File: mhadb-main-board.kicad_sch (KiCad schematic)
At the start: 62 parts, among them J1 Conn_01x04_Pin, J2 USB_C_Receptacle_USB2.0_14P, J3 Conn_01x04, J4 Conn_01x04, J5 Conn_01x04, J6 Conn_01x02, SW1 SW_Push, SW2 SW_Push, U1 ESP32-S3FN8, U2 SN65HVD230, U6 TPS5430DDA, U9 LDL212PV33R, Y1 48M

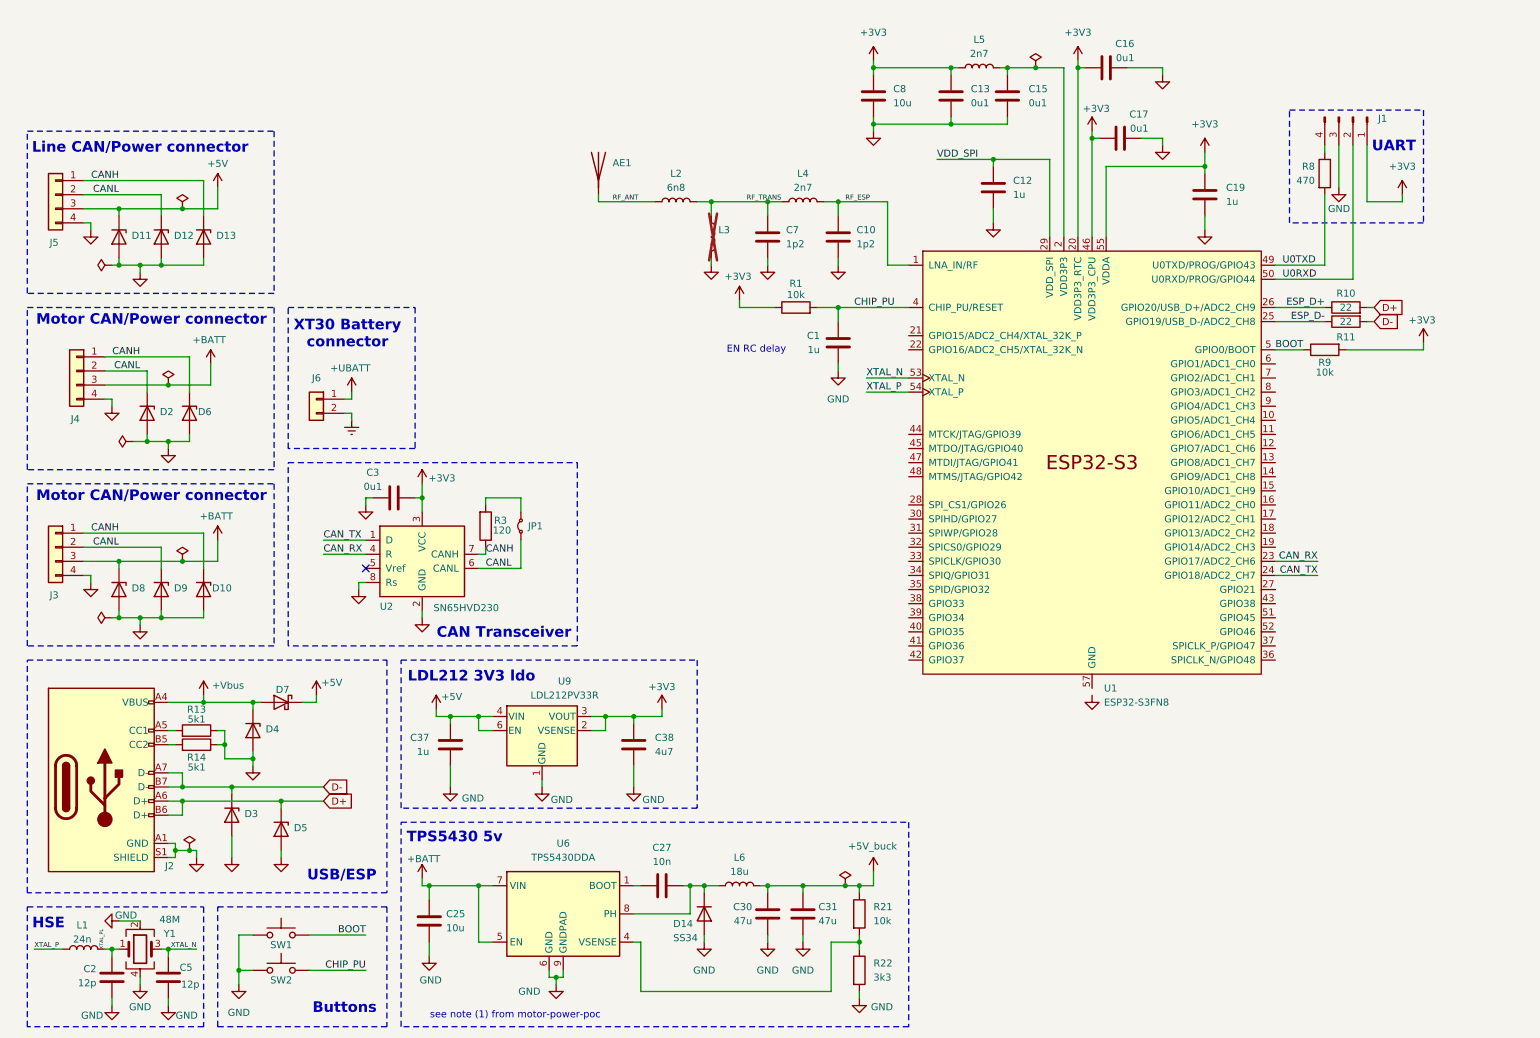
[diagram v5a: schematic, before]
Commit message: schem: import BQ77905 Battery protection
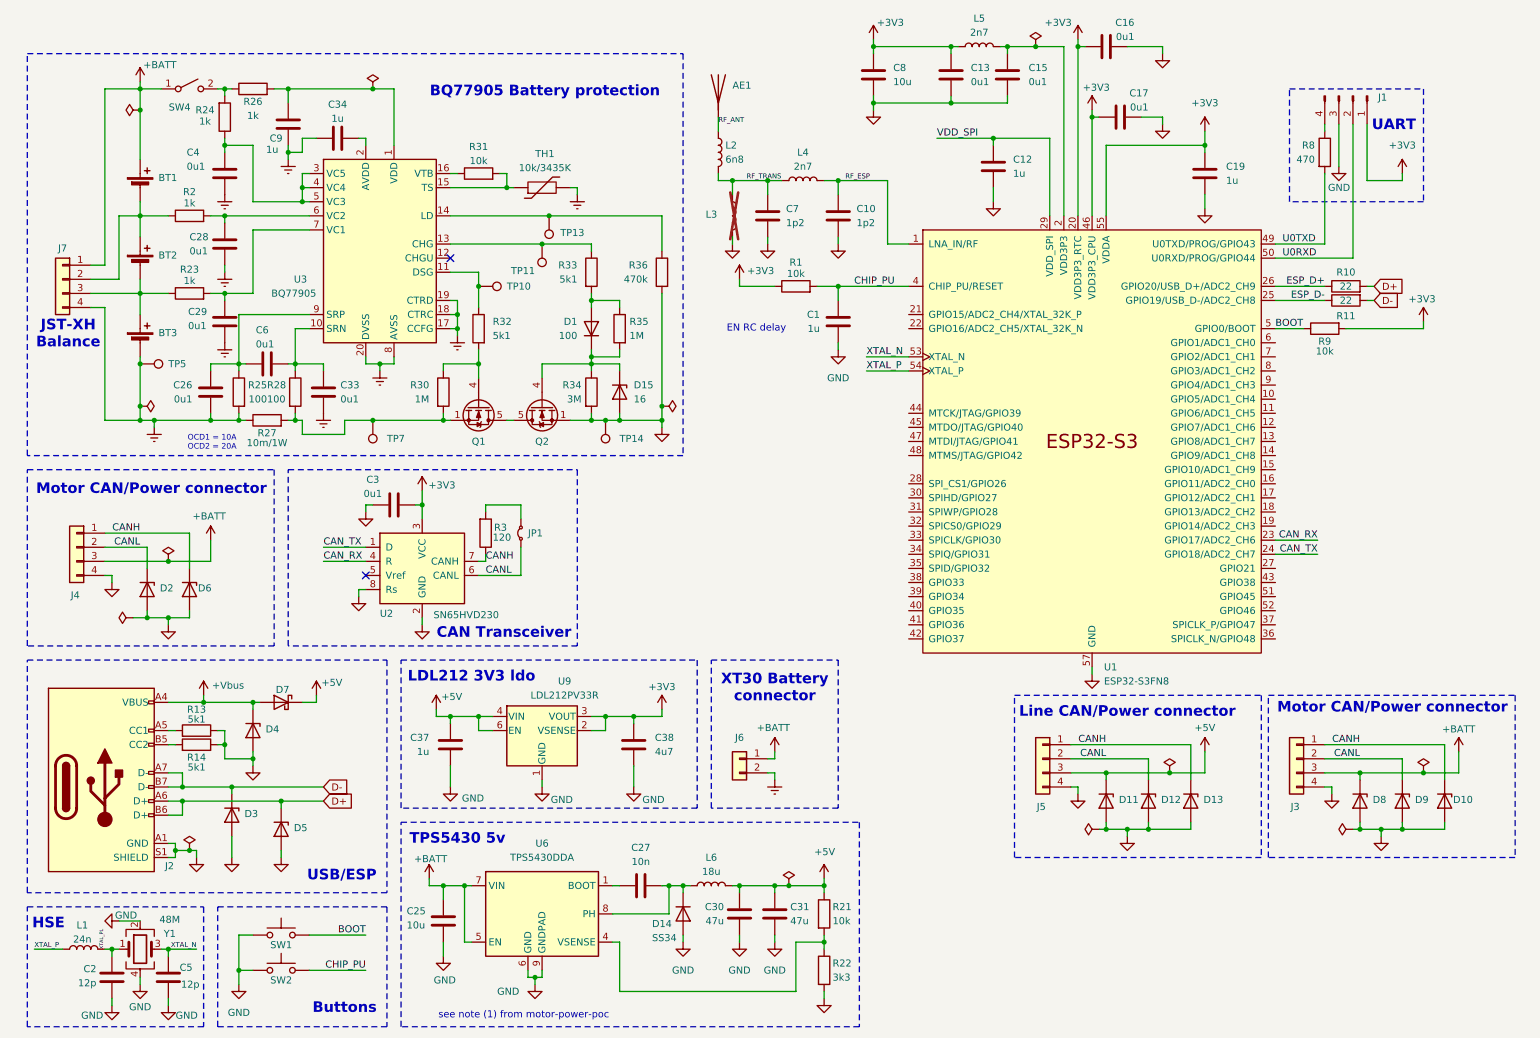
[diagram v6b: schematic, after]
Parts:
- added BT1, BT2, BT3: Battery_Cell, GLCS:BatteryHolder_MYOUNG_BH-18650-B1BA002, symbol Device:Battery_Cell
- added C26, C28, C29, C33, C4, C6: 0u1, Capacitor_SMD:C_0402_1005Metric, symbol Device:C
- added C34, C9: 1u, Capacitor_SMD:C_0402_1005Metric, symbol Device:C
- added D1: 100, Diode_SMD:D_SOD-323, symbol Device:D
- added D15: 16, Diode_SMD:D_SOD-123, symbol Device:D_Zener
- added J7: Conn_01x04, Connector_JST:JST_XH_B4B-XH-A_1x04_P2.50mm_Vertical, symbol Connector_Generic:Conn_01x04
- added Q1, Q2: Q_NMOS, Package_SO:Vishay_PowerPAK_1212-8_Single, symbol Transistor_FET:SiS454DN
- added R2, R23, R24, R26: 1k, Resistor_SMD:R_0402_1005Metric, symbol Device:R
- added R25, R28: 100, Resistor_SMD:R_0402_1005Metric, symbol Device:R
- added R27: 10m/1W, Resistor_SMD:R_1206_3216Metric, symbol Device:R
- added R30, R35: 1M, Resistor_SMD:R_0402_1005Metric, symbol Device:R
- added R31: 10k, Resistor_SMD:R_0402_1005Metric, symbol Device:R
- added R33: 5k1, Resistor_SMD:R_0402_1005Metric, symbol Device:R
- added R34: 3M, Resistor_SMD:R_0603_1608Metric, symbol Device:R
- added R36: 470k, Resistor_SMD:R_0603_1608Metric, symbol Device:R
- added SW4: SW_SPST, Connector_PinHeader_2.54mm:PinHeader_1x02_P2.54mm_Vertical, symbol Switch:SW_SPST
- added TH1: 10k/3435K, Connector_PinSocket_2.54mm:PinSocket_1x02_P2.54mm_Vertical, symbol Device:Thermistor
- added TP10, TP11, TP13, TP14, TP5, TP7: TestPoint, TestPoint:TestPoint_Pad_D2.0mm, symbol Connector:TestPoint
- added U3: BQ77905, Package_SO:TSSOP-20_4.4x6.5mm_P0.65mm, symbol GLCS:BQ77905
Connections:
- net +5V_buck is gone; now on net +5V: C30.1, C31.1, L6.2, R21.1
- net +UBATT is gone; now on net +BATT: J6.1 (Pin_1)
- net +BATT: now also BT1.1 (+), J7.1 (Pin_1), SW4.1 (A)
- net BGND: now also BT3.2 (-), C26.2, C28.2, C29.2, C33.2, C34.2, C4.2, C9.1, J7.4 (Pin_4), R25.2, R27.1, TH1.2, TP5.1, U3.17 (CCFG), U3.18 (CTRC), U3.19 (CTRD), U3.20 (DVSS), U3.8 (AVSS)
- net GND: now also U1.57 (GND), D15.2 (A), Q2.1 (S), Q2.2 (S), Q2.3 (S), R34.2, R36.2, TP14.1
- new net: D1.2 (A), R33.2, R35.1
- new net: D1.1 (K), D15.1 (K), Q2.4 (G), R34.1, R35.2
- new net: R14.1, TP10.1, U3.11 (DSG)
- new net: C4.1, R24.1, U3.3 (VC5), U3.4 (VC4), U3.5 (VC3)
- new net: Q1.4 (G), R14.2, R30.1
- new net: C33.1, C6.1, R28.1, U3.10 (SRN)
- new net: Q1.1 (S), Q1.2 (S), Q1.3 (S), R27.2, R28.2, R30.2, TP7.1
- new net: BT1.2 (-), BT2.1 (+), J7.2 (Pin_2), R2.1
- new net: BT2.2 (-), BT3.1 (+), J7.3 (Pin_3), R23.1
- new net: C34.1, U3.2 (AVDD)
- new net: C28.1, R2.2, U3.6 (VC2)
- new net: C29.1, R23.2, U3.7 (VC1)
- new net: R31.2, TH1.1, U3.15 (TS)
- new net: C26.1, C6.2, R25.1, U3.9 (SRP)
- new net: R31.1, U3.16 (VTB)
- new net: R33.1, TP11.1, U3.13 (CHG)
- new net: Q1.5 (D), Q2.5 (D)
- new net: R36.1, TP13.1, U3.14 (LD)
- new net: C9.2, R26.2, U3.1 (VDD)
- new net: R24.2, R26.1, SW4.2 (B)
- no-connect marks 1 -> 2
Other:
- note added: "BQ77905 Battery protection"
- note added: "JST-XH Balance"
- note added: "OCD1 = 10A OCD2 = 20A"
- moved on the sheet: AE1, C1, C10, C12, C13, C15, C16, C17, C19, C25, C27, C3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

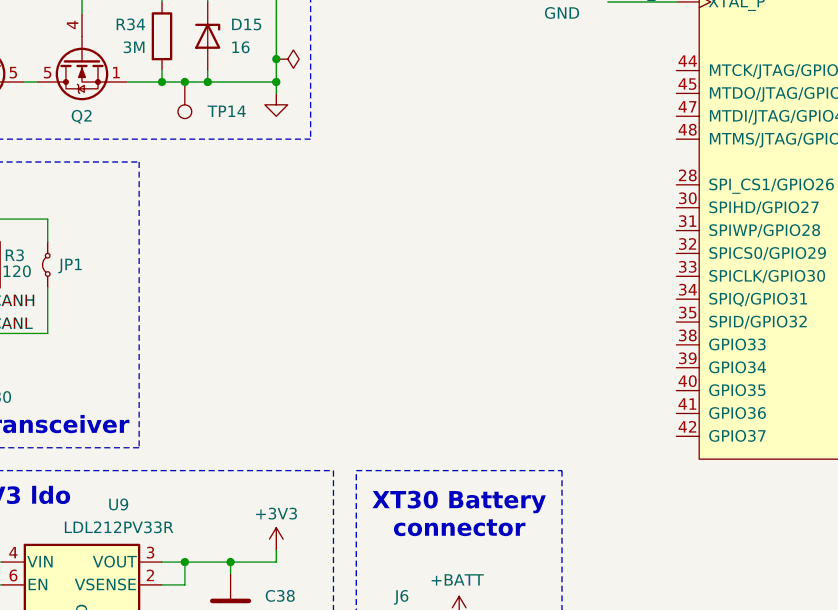
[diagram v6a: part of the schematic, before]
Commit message: schem: add passive buzzer
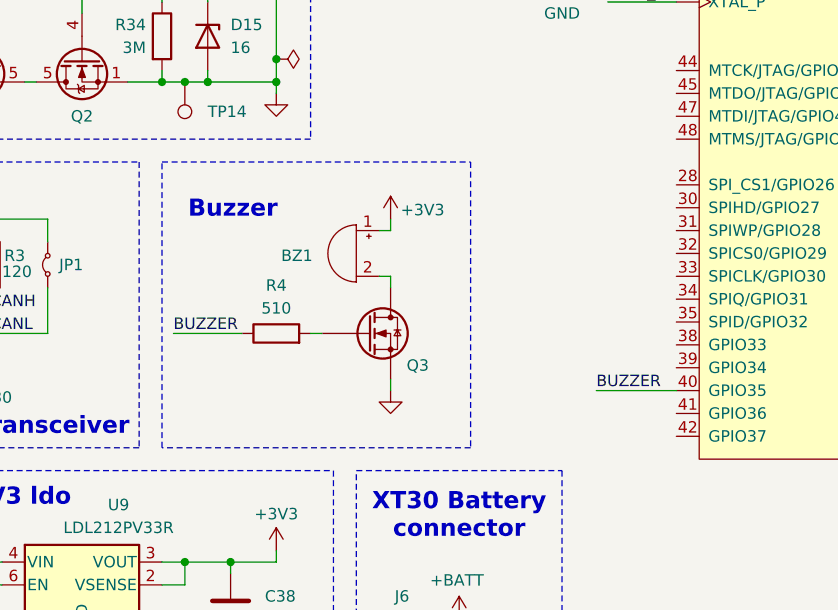
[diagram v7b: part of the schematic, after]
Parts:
- added BZ1: Buzzer, GLCS:MagneticBuzzer_Huaneng_MLT-5020, symbol Device:Buzzer
- added Q3: Q_NMOS, Package_TO_SOT_SMD:SOT-323_SC-70, symbol Device:Q_NMOS
- added R4: 510, Resistor_SMD:R_0402_1005Metric, symbol Device:R
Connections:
- net +3V3: now also BZ1.1 (+)
- net GND: now also Q3.2 (S)
- net BUZZER: now reaches U1.40 (GPIO35)
- net BUZZER: now also R4.1
- new net: BZ1.2 (-), Q3.3 (D)
- new net: Q3.1 (G), R4.2
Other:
- note added: "Buzzer"

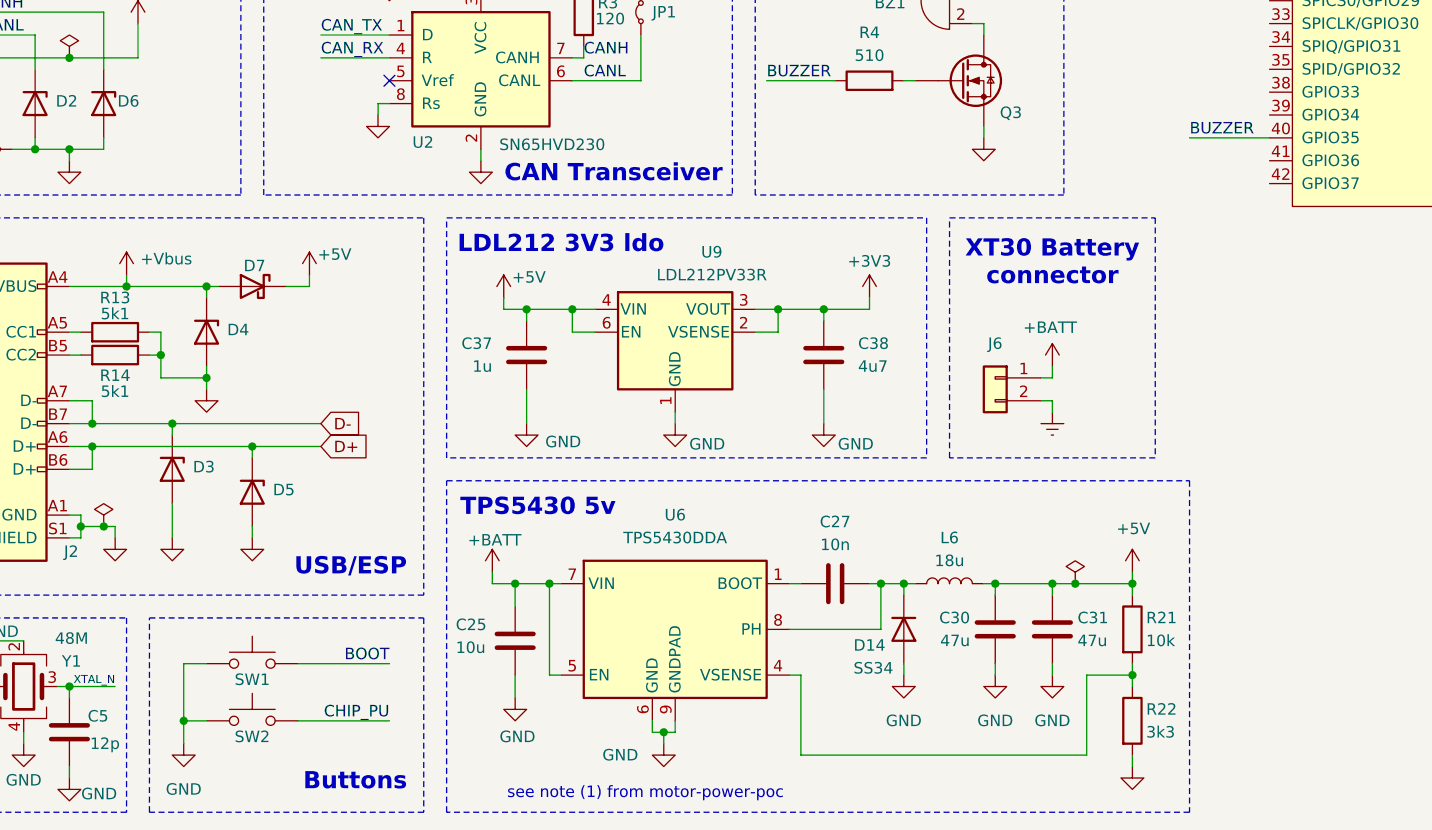
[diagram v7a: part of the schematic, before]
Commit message: schem: add EMS button
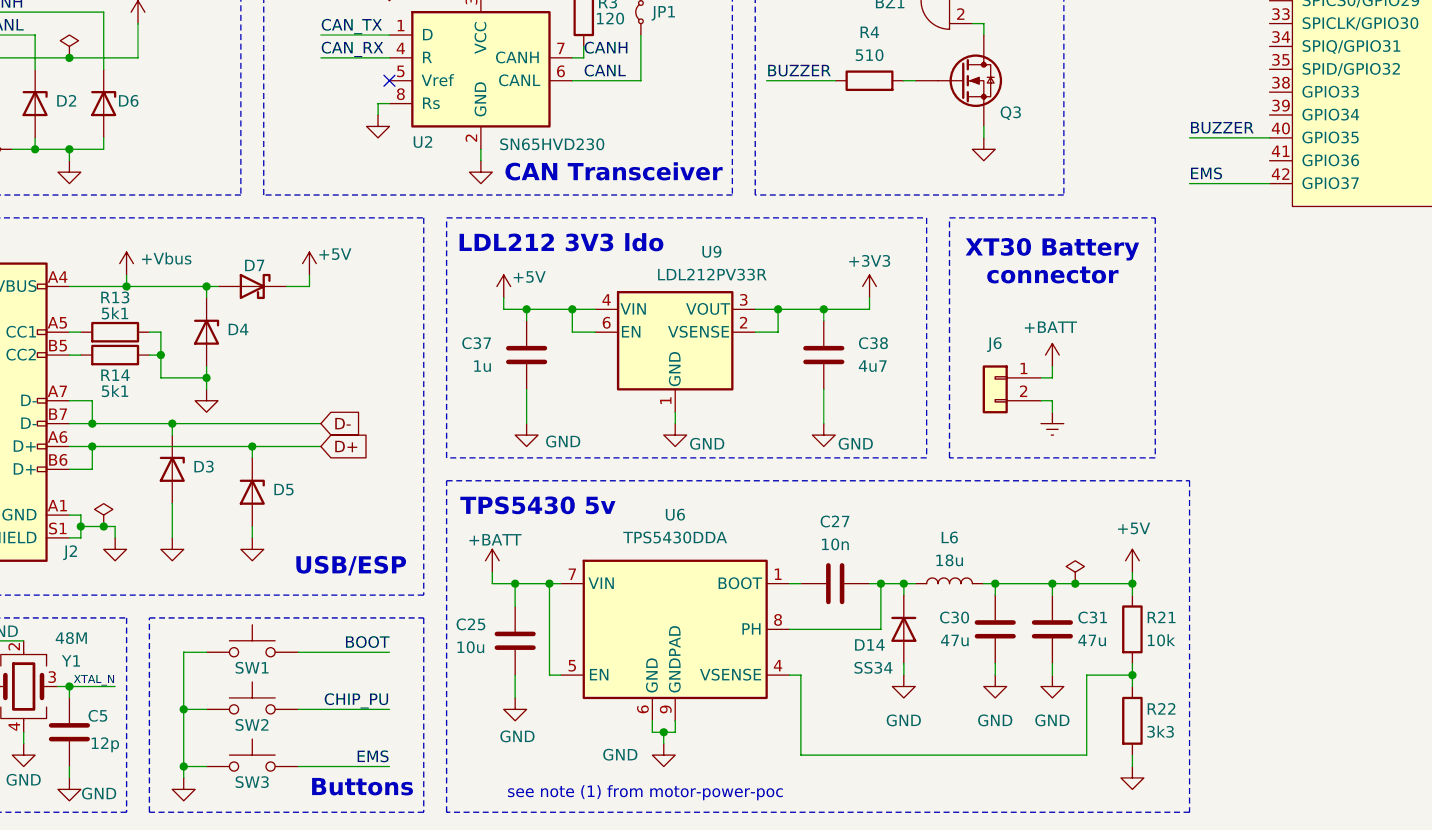
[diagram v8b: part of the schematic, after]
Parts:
- added SW3: SW_Push, Connector_JST:JST_PH_B2B-PH-K_1x02_P2.00mm_Vertical, symbol Switch:SW_Push
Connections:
- net GND: now also SW3.1
- net EMS: now reaches U1.42 (GPIO37)
- net EMS: now also SW3.2
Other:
- moved on the sheet: SW1, SW2
